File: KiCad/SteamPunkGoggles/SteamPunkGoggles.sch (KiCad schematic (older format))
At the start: 7 parts

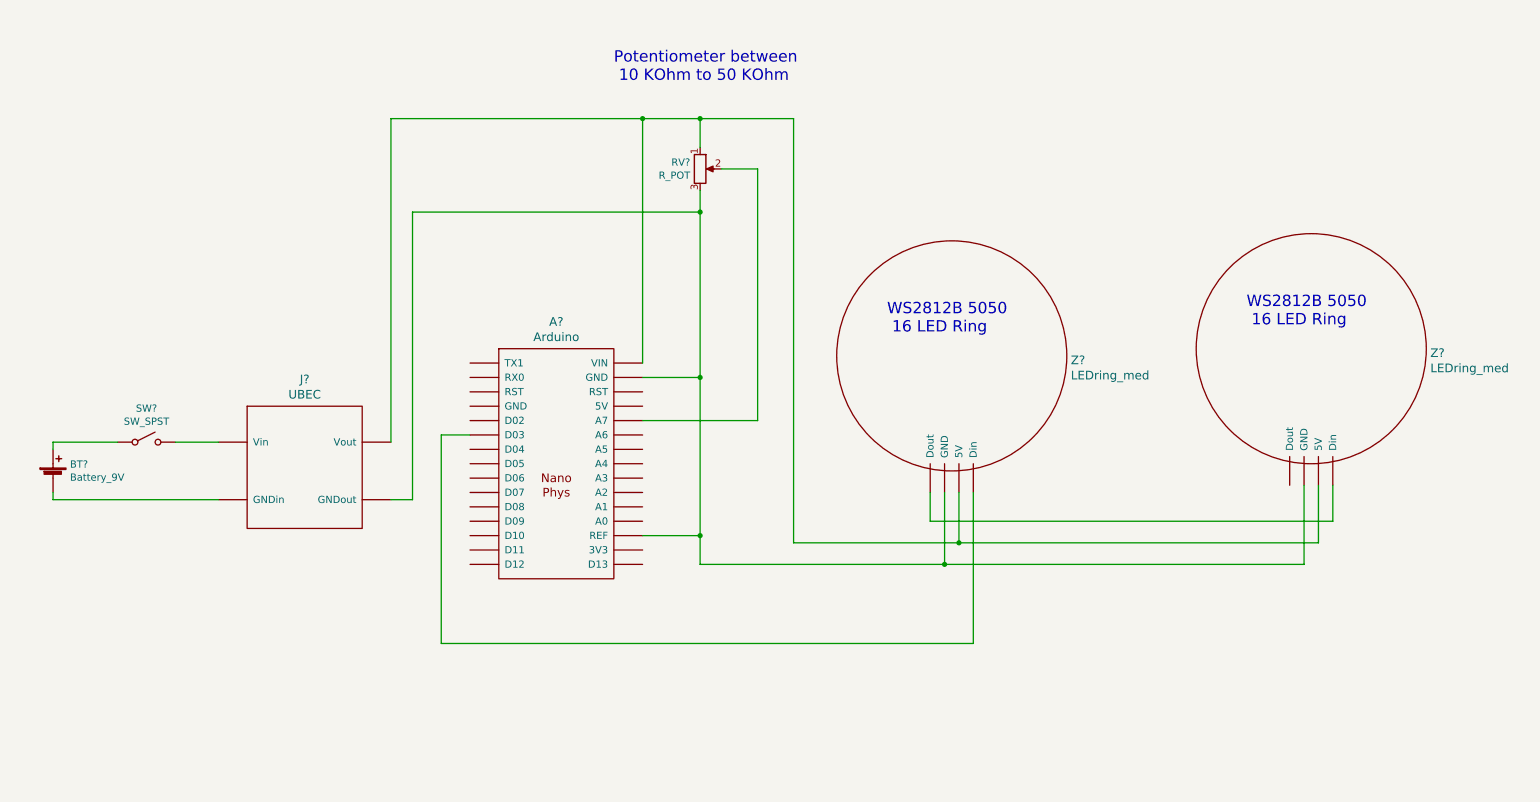
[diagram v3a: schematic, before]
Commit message: update schematic
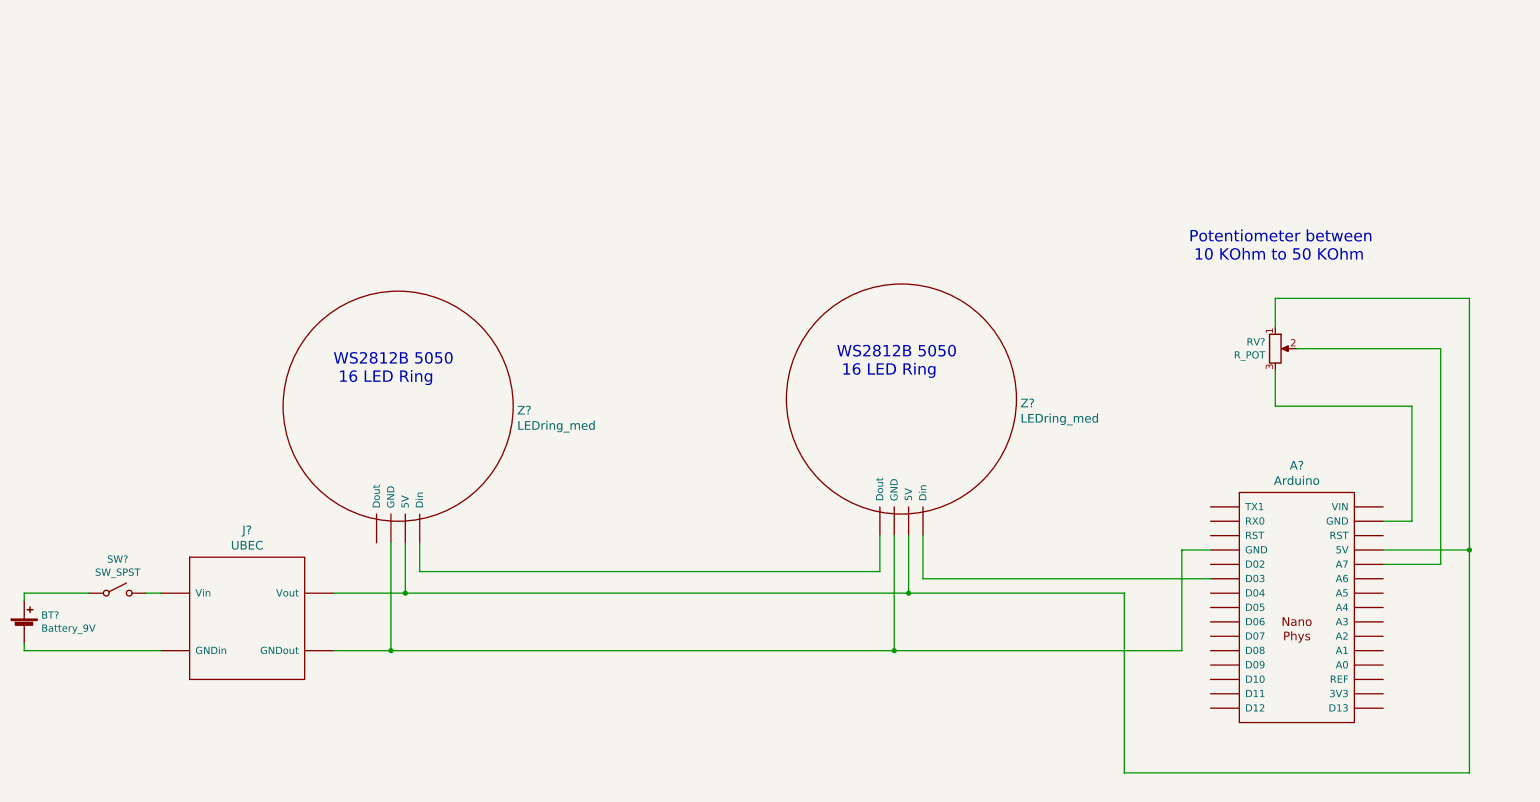
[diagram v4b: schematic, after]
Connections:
- net at A?.~ (VIN): now also Z?.~ (GND)
- net at Z?.~ (GND): now also Z?.~ (GND); no longer A?.~ (VIN)
- new net: A?.~ (VIN), J?.~ (Vout), RV?.1, Z?.~ (GND), Z?.~ (GND)
- new net: A?.~ (VIN), RV?.3
- new net: A?.~ (VIN), J?.~ (Vout), Z?.~ (GND), Z?.~ (GND)
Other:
- moved on the sheet: A?, BT?, RV?, SW?, Z?
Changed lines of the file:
@@
 L mdoLibrary:Arduino A?
 U 1 1 63D469A7
-P 4450 3950
-F 0 "A?" H 4450 4937 60  0000 C CNN
-F 1 "Arduino" H 4450 4831 60  0000 C CNN
-F 2 "" H 4450 3950 60  0000 C CNN
-F 3 "" H 4450 3950 60  0000 C CNN
-	1    4450 3950
+P 9600 4950
+F 0 "A?" H 9600 5937 60  0000 C CNN
+F 1 "Arduino" H 9600 5831 60  0000 C CNN
+F 2 "" H 9600 4950 60  0000 C CNN
+F 3 "" H 9600 4950 60  0000 C CNN
+	1    9600 4950
 	1    0    0    -1
 $EndComp
@@
 L mdoLibrary:UBEC J?
 U 1 1 63D4B50C
-P 2600 4050
-F 0 "J?" H 2700 4737 60  0000 C CNN
-F 1 "UBEC" H 2700 4631 60  0000 C CNN
-F 2 "" H 2600 4050 60  0001 C CNN
-F 3 "" H 2600 4050 60  0001 C CNN
-	1    2600 4050
+P 2200 5100
+F 0 "J?" H 2300 5787 60  0000 C CNN
+F 1 "UBEC" H 2300 5681 60  0000 C CNN
+F 2 "" H 2200 5100 60  0001 C CNN
+F 3 "" H 2200 5100 60  0001 C CNN
+	1    2200 5100
 	1    0    0    -1
 $EndComp
@@
 L Device:Battery_Cell BT?
 U 1 1 63D4C0E5
-P 950 4050
-F 0 "BT?" H 1068 4146 50  0000 L CNN
-F 1 "Battery_9V" H 1068 4055 50  0000 L CNN
-F 2 "" V 950 4110 50  0001 C CNN
-F 3 "~" V 950 4110 50  0001 C CNN
-	1    950  4050
+P 750 5100
+F 0 "BT?" H 868 5196 50  0000 L CNN
+F 1 "Battery_9V" H 868 5105 50  0000 L CNN
+F 2 "" V 750 5160 50  0001 C CNN
+F 3 "~" V 750 5160 50  0001 C CNN
+	1    750  5100
 	1    0    0    -1
 $EndComp
 Wire Wire Line
-	5450 2200 5450 3350
-Wire Wire Line
-	5450 3350 5050 3350
-Wire Wire Line
-	5450 1550 5450 1750
+	9450 2800 9450 3000
 $Comp
 L Device:R_POT RV?
 U 1 1 63D49A93
-P 5450 1900
-F 0 "RV?" H 5381 1946 50  0000 R CNN
-F 1 "R_POT" H 5381 1855 50  0000 R CNN
-F 2 "" H 5450 1900 50  0001 C CNN
-F 3 "~" H 5450 1900 50  0001 C CNN
-	1    5450 1900
+P 9450 3150
+F 0 "RV?" H 9381 3196 50  0000 R CNN
+F 1 "R_POT" H 9381 3105 50  0000 R CNN
+F 2 "" H 9450 3150 50  0001 C CNN
+F 3 "~" H 9450 3150 50  0001 C CNN
+	1    9450 3150
 	1    0    0    -1
 $EndComp
 Wire Wire Line
-	5450 2050 5450 2200
-Connection ~ 5450 2200
+	750  4850 750  4900
 Wire Wire Line
-	5450 1550 5050 1550
-Connection ~ 5050 1550
-Wire Wire Line
-	5600 1900 5850 1900
-Wire Wire Line
-	5850 1900 5850 3650
-Wire Wire Line
-	5450 4450 5050 4450
-Connection ~ 5450 3350
-Wire Wire Line
-	3850 3750 3650 3750
-Wire Wire Line
-	3650 3750 3650 5200
-Wire Wire Line
-	5450 1550 6100 1550
-Connection ~ 5450 1550
-Wire Wire Line
-	3450 2200 3450 4200
-Wire Wire Line
-	950  3800 950  3850
-Wire Wire Line
-	950  4200 950  4150
+	750  5250 750  5200
 $Comp
 L mdoLibrary:SW_SPST SW?
 U 1 1 63D6255A
-P 1600 3800
-F 0 "SW?" H 1600 4035 50  0000 C CNN
-F 1 "SW_SPST" H 1600 3944 50  0000 C CNN
-F 2 "" H 1600 3800 50  0001 C CNN
-F 3 "" H 1600 3800 50  0001 C CNN
-	1    1600 3800
+P 1400 4850
+F 0 "SW?" H 1400 5085 50  0000 C CNN
+F 1 "SW_SPST" H 1400 4994 50  0000 C CNN
+F 2 "" H 1400 4850 50  0001 C CNN
+F 3 "" H 1400 4850 50  0001 C CNN
+	1    1400 4850
 	1    0    0    -1
 $EndComp
 Wire Wire Line
-	3300 3800 3300 1550
-Wire Wire Line
-	3300 1550 5050 1550
-Wire Wire Line
-	3300 4200 3450 4200
-Wire Wire Line
-	1800 3800 2100 3800
-Wire Wire Line
-	1400 3800 950  3800
-Wire Wire Line
-	950  4200 2100 4200
-Wire Wire Line
-	3650 5200 7350 5200
-Wire Wire Line
-	5450 4450 5450 4650
-Connection ~ 5450 4450
-Wire Wire Line
-	6100 1550 6100 4500
+	1200 4850 750  4850
 $Comp
 L mdoLibrary:LEDring_med Z?
 U 1 1 63D744C6
-P 7200 3200
-F 0 "Z?" H 8028 3170 60  0000 L CNN
-F 1 "LEDring_med" H 8028 3064 60  0000 L CNN
-F 2 "" H 7200 3350 60  0001 C CNN
-F 3 "" H 7200 3350 60  0001 C CNN
-	1    7200 3200
+P 3350 3550
+F 0 "Z?" H 4178 3520 60  0000 L CNN
+F 1 "LEDring_med" H 4178 3414 60  0000 L CNN
+F 2 "" H 3350 3700 60  0001 C CNN
+F 3 "" H 3350 3700 60  0001 C CNN
+	1    3350 3550
 	1    0    0    -1
 $EndComp
@@
 L mdoLibrary:LEDring_med Z?
 U 1 1 63D74B09
-P 9700 3150
-F 0 "Z?" H 10528 3120 60  0000 L CNN
-F 1 "LEDring_med" H 10528 3014 60  0000 L CNN
-F 2 "" H 9700 3300 60  0001 C CNN
-F 3 "" H 9700 3300 60  0001 C CNN
-	1    9700 3150
+P 6850 3500
+F 0 "Z?" H 7678 3470 60  0000 L CNN
+F 1 "LEDring_med" H 7678 3364 60  0000 L CNN
+F 2 "" H 6850 3650 60  0001 C CNN
+F 3 "" H 6850 3650 60  0001 C CNN
+	1    6850 3500
 	1    0    0    -1
 $EndComp
 Wire Wire Line
-	5450 4650 7150 4650
+	3400 4500 3400 4850
 Wire Wire Line
-	7250 4150 7250 4500
-Connection ~ 7250 4500
-Wire Wire Line
-	7250 4500 9750 4500
-Wire Wire Line
-	7050 4150 7050 4350
-Wire Wire Line
-	6100 4500 7250 4500
-Wire Wire Line
-	7150 4150 7150 4650
-Connection ~ 7150 4650
-Wire Wire Line
-	7150 4650 9650 4650
-Wire Wire Line
-	9650 4100 9650 4650
-Wire Wire Line
-	9750 4100 9750 4500
-Wire Wire Line
-	9850 4100 9850 4350
-Text Notes 6750 3050 0    79   ~ 0
+	6900 4450 6900 4850
+Text Notes 2900 3400 0    79   ~ 0
 WS2812B 5050\n 16 LED Ring
-Text Notes 9250 3000 0    79   ~ 0
+Text Notes 6400 3350 0    79   ~ 0
 WS2812B 5050\n 16 LED Ring
-Text Notes 4850 1300 0    79   ~ 0
+Text Notes 8850 2550 0    79   ~ 0
 Potentiometer between\n 10 KOhm to 50 KOhm
 Wire Wire Line
-	7050 4350 9850 4350
+	3400 4850 6900 4850
 Wire Wire Line
-	7350 4150 7350 5200
+	6700 4450 6700 4700
 Wire Wire Line
-	5050 1550 5050 3250
+	6700 4700 3500 4700
 Wire Wire Line
-	3450 2200 5450 2200
+	3500 4500 3500 4700
 Wire Wire Line
-	5050 3650 5850 3650
+	9000 4750 7000 4750
 Wire Wire Line
-	5450 3350 5450 4450
+	7000 4450 7000 4750
+Wire Wire Line
+	10600 3150 10600 4650
+Wire Wire Line
+	10600 4650 10200 4650
+Wire Wire Line
+	9600 3150 10600 3150
+Wire Wire Line
+	6900 4850 8400 4850
+Wire Wire Line
+	8400 4850 8400 6100
+Connection ~ 6900 4850
+Wire Wire Line
+	1700 4850 1600 4850
+Wire Wire Line
+	1700 5250 750  5250
+Connection ~ 3400 4850
+Wire Wire Line
+	2900 5250 3300 5250
+Wire Wire Line
+	9450 3300 9450 3550
+Wire Wire Line
+	8800 4550 9000 4550
+Wire Wire Line
+	10800 2800 10800 4550
+Wire Wire Line
+	8400 6100 10800 6100
+Connection ~ 10800 4550
+Wire Wire Line
+	10800 4550 10800 6100
+Wire Wire Line
+	9450 2800 10800 2800
+Wire Wire Line
+	10200 4550 10800 4550
+Wire Wire Line
+	10200 4350 10400 4350
+Wire Wire Line
+	10400 4350 10400 3550
+Wire Wire Line
+	9450 3550 10400 3550
+Wire Wire Line
+	2900 4850 3400 4850
+Wire Wire Line
+	3300 5250 6800 5250
+Connection ~ 3300 5250
+Wire Wire Line
+	3300 4500 3300 5250
+Connection ~ 6800 5250
+Wire Wire Line
+	6800 5250 8800 5250
+Wire Wire Line
+	6800 4450 6800 5250
+Wire Wire Line
+	8800 4550 8800 5250
 $EndSCHEMATC

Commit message: update schematic
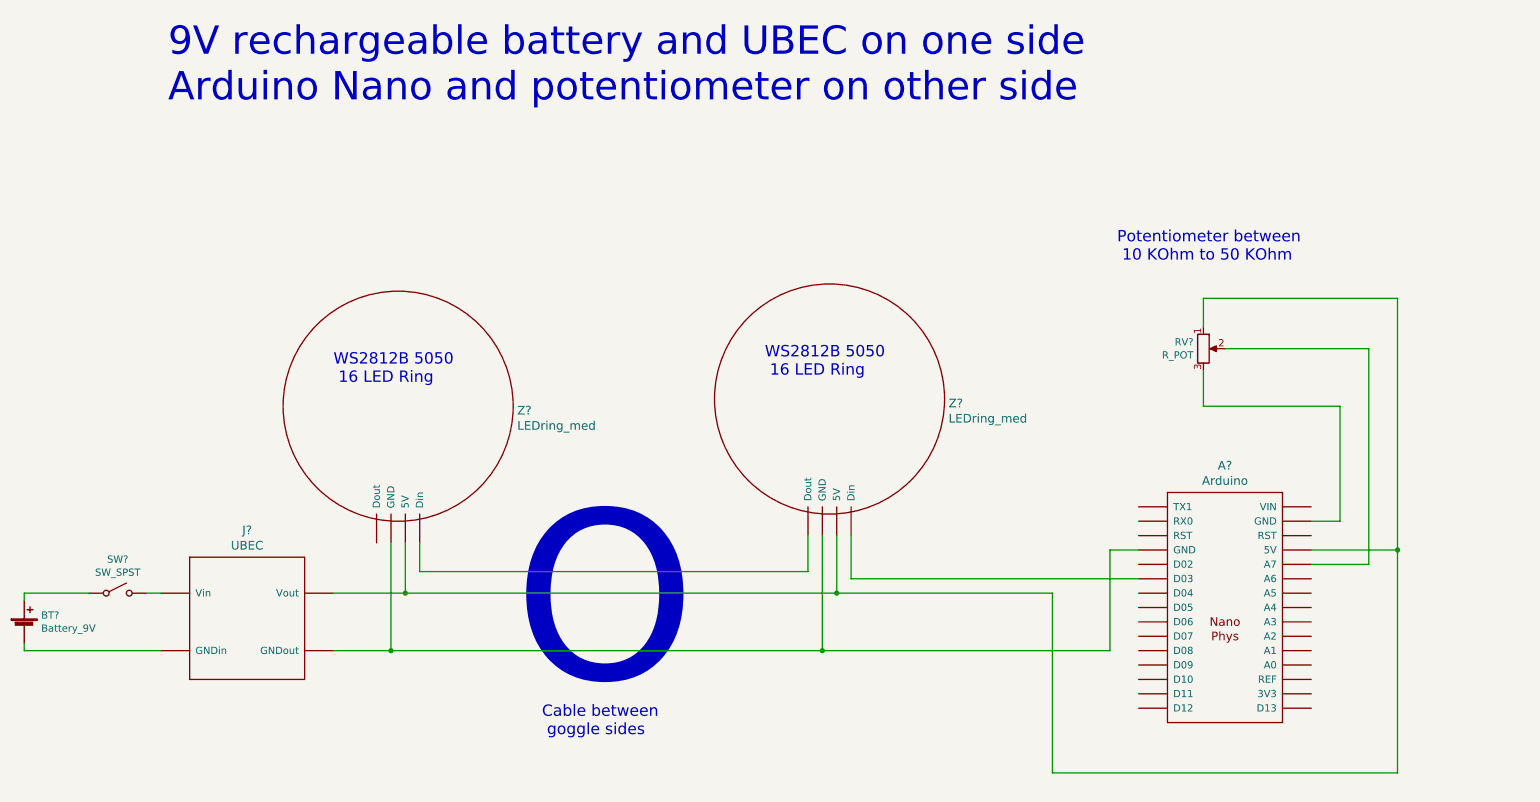
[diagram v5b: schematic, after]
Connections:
- net at A?.~ (VIN): now also Z?.~ (GND)
- net at Z?.~ (GND), Z?.~ (GND): no longer A?.~ (VIN), J?.~ (Vout)
- new net: A?.~ (VIN), J?.~ (Vout), RV?.1, Z?.~ (GND), Z?.~ (GND)
- new net: A?.~ (VIN), J?.~ (Vout), Z?.~ (GND), Z?.~ (GND)
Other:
- note added: "9V rechargeable battery and UBEC on one side\nArduino Nano and potentiometer on other side"
- note added: "Cable between\n goggle sides"
- note added: "O"
- moved on the sheet: A?, RV?, Z?
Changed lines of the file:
@@
 EELAYER 30 0
 EELAYER END
-$Descr A4 11693 8268
+$Descr A 11000 8500
 encoding utf-8
 Sheet 1 1
@@
 L mdoLibrary:Arduino A?
 U 1 1 63D469A7
-P 9600 4950
-F 0 "A?" H 9600 5937 60  0000 C CNN
-F 1 "Arduino" H 9600 5831 60  0000 C CNN
-F 2 "" H 9600 4950 60  0000 C CNN
-F 3 "" H 9600 4950 60  0000 C CNN
-	1    9600 4950
+P 9100 4950
+F 0 "A?" H 9100 5937 60  0000 C CNN
+F 1 "Arduino" H 9100 5831 60  0000 C CNN
+F 2 "" H 9100 4950 60  0000 C CNN
+F 3 "" H 9100 4950 60  0000 C CNN
+	1    9100 4950
 	1    0    0    -1
 $EndComp
@@
 $EndComp
 Wire Wire Line
-	9450 2800 9450 3000
+	8950 2800 8950 3000
 $Comp
 L Device:R_POT RV?
 U 1 1 63D49A93
-P 9450 3150
-F 0 "RV?" H 9381 3196 50  0000 R CNN
-F 1 "R_POT" H 9381 3105 50  0000 R CNN
-F 2 "" H 9450 3150 50  0001 C CNN
-F 3 "~" H 9450 3150 50  0001 C CNN
-	1    9450 3150
+P 8950 3150
+F 0 "RV?" H 8881 3196 50  0000 R CNN
+F 1 "R_POT" H 8881 3105 50  0000 R CNN
+F 2 "" H 8950 3150 50  0001 C CNN
+F 3 "~" H 8950 3150 50  0001 C CNN
+	1    8950 3150
 	1    0    0    -1
 $EndComp
@@
 L mdoLibrary:LEDring_med Z?
 U 1 1 63D74B09
-P 6850 3500
-F 0 "Z?" H 7678 3470 60  0000 L CNN
-F 1 "LEDring_med" H 7678 3364 60  0000 L CNN
-F 2 "" H 6850 3650 60  0001 C CNN
-F 3 "" H 6850 3650 60  0001 C CNN
-	1    6850 3500
+P 6350 3500
+F 0 "Z?" H 7178 3470 60  0000 L CNN
+F 1 "LEDring_med" H 7178 3364 60  0000 L CNN
+F 2 "" H 6350 3650 60  0001 C CNN
+F 3 "" H 6350 3650 60  0001 C CNN
+	1    6350 3500
 	1    0    0    -1
 $EndComp
@@
 	3400 4500 3400 4850
 Wire Wire Line
-	6900 4450 6900 4850
+	6400 4450 6400 4850
 Text Notes 2900 3400 0    79   ~ 0
 WS2812B 5050\n 16 LED Ring
-Text Notes 6400 3350 0    79   ~ 0
+Text Notes 5900 3350 0    79   ~ 0
 WS2812B 5050\n 16 LED Ring
-Text Notes 8850 2550 0    79   ~ 0
+Text Notes 8350 2550 0    79   ~ 0
 Potentiometer between\n 10 KOhm to 50 KOhm
 Wire Wire Line
-	3400 4850 6900 4850
+	2900 4850 3400 4850
 Wire Wire Line
-	6700 4450 6700 4700
+	6200 4450 6200 4700
 Wire Wire Line
-	6700 4700 3500 4700
+	6200 4700 3500 4700
 Wire Wire Line
 	3500 4500 3500 4700
 Wire Wire Line
-	9000 4750 7000 4750
+	8500 4750 6500 4750
 Wire Wire Line
-	7000 4450 7000 4750
+	6500 4450 6500 4750
 Wire Wire Line
-	10600 3150 10600 4650
+	10100 3150 10100 4650
 Wire Wire Line
-	10600 4650 10200 4650
+	10100 4650 9700 4650
 Wire Wire Line
-	9600 3150 10600 3150
+	9100 3150 10100 3150
 Wire Wire Line
-	6900 4850 8400 4850
+	6400 4850 7900 4850
 Wire Wire Line
-	8400 4850 8400 6100
-Connection ~ 6900 4850
+	7900 4850 7900 6100
+Connection ~ 6400 4850
 Wire Wire Line
 	1700 4850 1600 4850
@@
 Connection ~ 3400 4850
 Wire Wire Line
-	2900 5250 3300 5250
+	8950 3300 8950 3550
 Wire Wire Line
-	9450 3300 9450 3550
+	8300 4550 8500 4550
 Wire Wire Line
-	8800 4550 9000 4550
+	10300 2800 10300 4550
 Wire Wire Line
-	10800 2800 10800 4550
+	7900 6100 10300 6100
+Connection ~ 10300 4550
 Wire Wire Line
-	8400 6100 10800 6100
-Connection ~ 10800 4550
+	10300 4550 10300 6100
 Wire Wire Line
-	10800 4550 10800 6100
+	8950 2800 10300 2800
 Wire Wire Line
-	9450 2800 10800 2800
+	9700 4550 10300 4550
 Wire Wire Line
-	10200 4550 10800 4550
+	9700 4350 9900 4350
 Wire Wire Line
-	10200 4350 10400 4350
+	9900 4350 9900 3550
 Wire Wire Line
-	10400 4350 10400 3550
-Wire Wire Line
-	9450 3550 10400 3550
-Wire Wire Line
-	2900 4850 3400 4850
-Wire Wire Line
-	3300 5250 6800 5250
-Connection ~ 3300 5250
+	8950 3550 9900 3550
 Wire Wire Line
 	3300 4500 3300 5250
-Connection ~ 6800 5250
+Connection ~ 6300 5250
 Wire Wire Line
-	6800 5250 8800 5250
+	6300 5250 8300 5250
 Wire Wire Line
-	6800 4450 6800 5250
+	6300 4450 6300 5250
 Wire Wire Line
-	8800 4550 8800 5250
+	8300 4550 8300 5250
+Wire Wire Line
+	3400 4850 6400 4850
+Wire Wire Line
+	3300 5250 6300 5250
+Wire Wire Line
+	2900 5250 3300 5250
+Connection ~ 3300 5250
+Text Notes 4150 5600 0    1181 ~ 0
+O
+Text Notes 4350 5850 0    79   ~ 0
+Cable between\n goggle sides
+Text Notes 1750 1450 0    197  ~ 0
+9V rechargeable battery and UBEC on one side\nArduino Nano and potentiometer on other side
 $EndSCHEMATC

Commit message: annotate schematic
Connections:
- net at A?.~ (VIN): now also Z?.~ (GND)
- net at Z?.~ (GND), Z?.~ (GND): no longer A?.~ (VIN), J?.~ (Vout)
- new net: A?.~ (VIN), J?.~ (Vout), RV?.1, Z?.~ (GND), Z?.~ (GND)
- new net: A?.~ (VIN), J?.~ (Vout), Z?.~ (GND), Z?.~ (GND)
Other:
- note added: "5 Volt\nUniversal\nBattery\nEliminator\nCircuit"
- note added: "9V Battery"
- note added: "Knife Switch"
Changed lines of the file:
@@
 Sheet 1 1
 Title "Steam Punk Goggles from KnowHow187"
-Date "2023-01-27"
+Date "2023-02-03"
 Rev ""
 Comp "MDO"
@@
 	2900 5250 3300 5250
 Connection ~ 3300 5250
-Text Notes 4150 5600 0    1181 ~ 0
-O
-Text Notes 4350 5850 0    79   ~ 0
+Text Notes 4350 5950 0    79   ~ 0
 Cable between\n goggle sides
 Text Notes 1750 1450 0    197  ~ 0
 9V rechargeable battery and UBEC on one side\nArduino Nano and potentiometer on other side
+Wire Bus Line
+	4350 4350 5250 4350
+Text Notes 3750 5650 0    1220 ~ 0
+O
+Text Notes 4600 5650 0    1220 ~ 0
+O
+Wire Bus Line
+	4350 5600 5250 5600
+Text Notes 1050 4550 0    79   ~ 0
+Knife Switch
+Text Notes 2000 6100 0    79   ~ 0
+5 Volt\nUniversal\nBattery\nEliminator\nCircuit
+Text Notes 750  5400 0    79   ~ 0
+9V Battery
 $EndSCHEMATC
